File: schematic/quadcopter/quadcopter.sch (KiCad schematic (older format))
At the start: 17 parts, among them SW1 SW_SPST, U1 WEACT_STM32F411CEU6, U10 iFlight_XING_E_2207, U11 HAKRC_35A_ESC, U12 iFlight_XING_E_2207, U13 iFlight_XING_E_2207, U14 iFlight_XING_E_2207, U2 SPARKRUN_ICM-20948, U3 LIPO_Battery_4CELL, U4 FS-A8S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

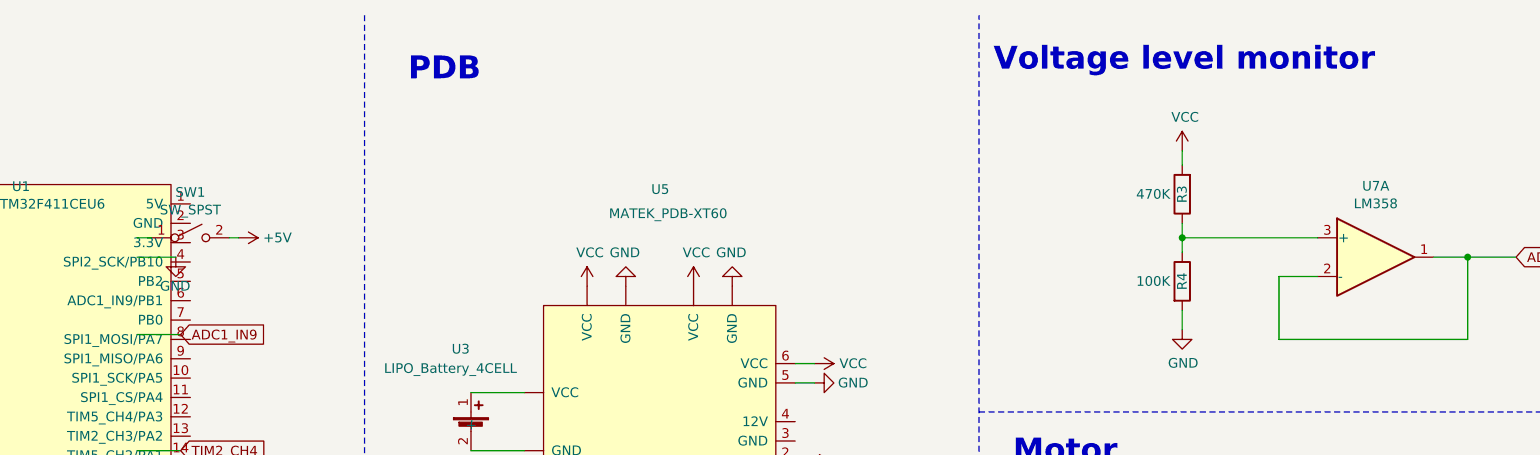
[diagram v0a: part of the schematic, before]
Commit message: Update voltage monitor
- delete moving average filter
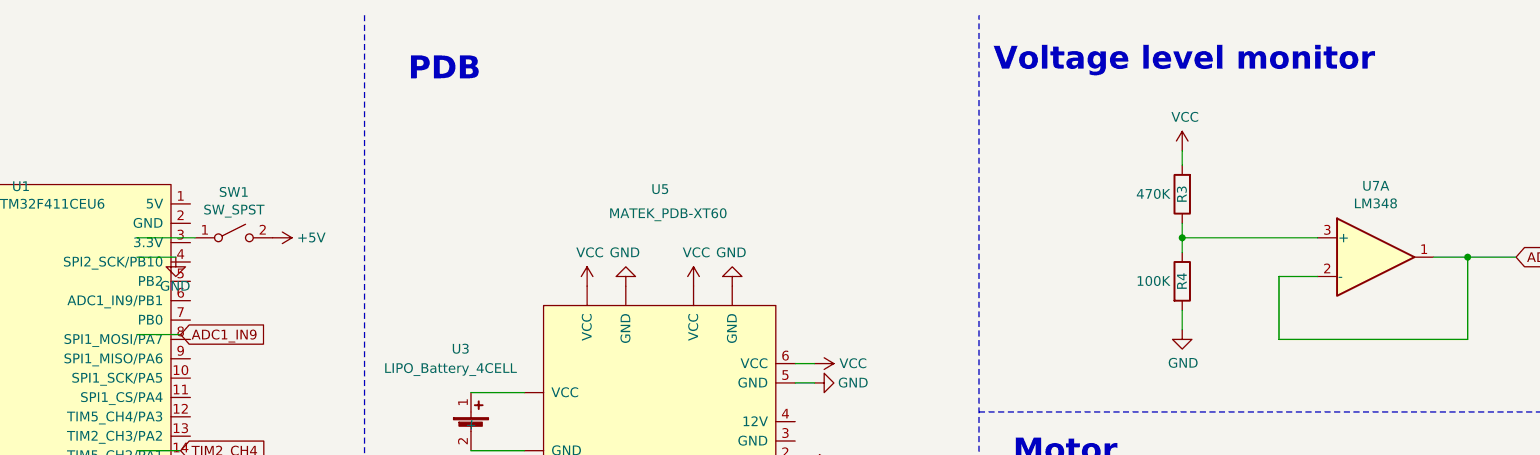
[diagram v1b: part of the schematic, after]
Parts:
- U7: value LM358 -> LM348
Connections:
- wire segments 75 -> 74
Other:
- moved on the sheet: SW1
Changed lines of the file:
@@
 L power:+5V #PWR0103
 U 1 1 606BF20D
-P 3150 1625
-F 0 "#PWR0103" H 3150 1475 50  0001 C CNN
-F 1 "+5V" V 3150 1825 50  0000 C CNN
-F 2 "" H 3150 1625 50  0001 C CNN
-F 3 "" H 3150 1625 50  0001 C CNN
-	1    3150 1625
+P 3325 1625
+F 0 "#PWR0103" H 3325 1475 50  0001 C CNN
+F 1 "+5V" V 3325 1825 50  0000 C CNN
+F 2 "" H 3325 1625 50  0001 C CNN
+F 3 "" H 3325 1625 50  0001 C CNN
+	1    3325 1625
 	0    1    1    0
 $EndComp
@@
 L Switch:SW_SPST SW1
 U 1 1 6075AD94
-P 2900 1625
-F 0 "SW1" H 2900 1860 50  0000 C CNN
-F 1 "SW_SPST" H 2900 1769 50  0000 C CNN
-F 2 "" H 2900 1625 50  0001 C CNN
-F 3 "~" H 2900 1625 50  0001 C CNN
-	1    2900 1625
-	1    0    0    -1
-$EndComp
-Wire Wire Line
-	2625 1625 2700 1625
-Wire Wire Line
-	3100 1625 3150 1625
+P 3125 1625
+F 0 "SW1" H 3125 1860 50  0000 C CNN
+F 1 "SW_SPST" H 3125 1769 50  0000 C CNN
+F 2 "" H 3125 1625 50  0001 C CNN
+F 3 "~" H 3125 1625 50  0001 C CNN
+	1    3125 1625
+	1    0    0    -1
+$EndComp
+Wire Wire Line
+	2625 1625 2925 1625
 Wire Wire Line
 	2625 1725 2825 1725
@@
 P 9025 1725
 F 0 "U7" H 9025 2092 50  0000 C CNN
-F 1 "LM358" H 9025 2001 50  0000 C CNN
+F 1 "LM348" H 9025 2001 50  0000 C CNN
 F 2 "" H 9025 1725 50  0001 C CNN
 F 3 "http://www.ti.com/lit/ds/symlink/lm2904-n.pdf" H 9025 1725 50  0001 C CNN

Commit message: Update FMU schematic
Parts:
- removed R3: 470K, symbol Device:R
- removed R4: 100K, symbol Device:R
- removed U1: WEACT_STM32F411CEU6, symbol quadcopter_symbol:WEACT_STM32F411CEU6
- removed U11, U6: HAKRC_35A_ESC, symbol quadcopter_symbol:HAKRC_35A_ESC
- removed U14: iFlight_XING_E_2207, symbol quadcopter_symbol:iFlight_XING_E_2207
- removed U2: SPARKRUN_ICM-20948, symbol quadcopter_symbol:SPARKRUN_ICM-20948
- removed U3: LIPO_Battery_4CELL, symbol quadcopter_symbol:LIPO_Battery_4CELL
- removed U4: FS-A8S, symbol quadcopter_symbol:FS-A8S
- removed U5: MATEK_PDB-XT60, symbol quadcopter_symbol:MATEK_PDB-XT60
- removed U7: LM348, symbol Amplifier_Operational:LM358
- added BZ1: Buzzer, symbol Device:Buzzer
- added R1: 470K, symbol Device:R
- added R2: 100K, symbol Device:R
- added U1: MATEK_PDB-XT60, symbol quadcopter_symbol:MATEK_PDB-XT60
- added U11: iFlight_XING_E_2207, symbol quadcopter_symbol:iFlight_XING_E_2207
- added U2: nRF24L01+PA+LNA_BreakOut, symbol quadcopter_symbol:nRF24L01+PA+LNA_BreakOut
- added U3: LM358N, symbol quadcopter_symbol:LM358N
- added U4: WEACT_STM32F411CEU6, symbol quadcopter_symbol:WEACT_STM32F411CEU6
- added U5, U7: HAKRC_35A_ESC, symbol quadcopter_symbol:HAKRC_35A_ESC
- added U6: ICM_20948_BreakOut, symbol quadcopter_symbol:ICM_20948_BreakOut
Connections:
- net labels added: +BATT, SWO
- net labels removed: +5V, ADC1_IN9, CS, MISO, MOSI, SCLK, SPI1_CS, SPI1_MISO, SPI1_MOSI, SPI1_SCLK, TIM2_CH3, TIM2_CH4, TIM5_CH1, TIM5_CH2, USART1_RX
- wire segments 74 -> 113
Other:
- note removed: "IMU (ICM-20948)"
- note removed: "MCU module"
- note removed: "Motor"
- note removed: "Motor 1"
- note removed: "Motor 2"
- note removed: "Motor 3"
- note removed: "Motor 4"
- note removed: "PDB"
- note removed: "RC Receiver (FS-A8S)"
- note removed: "Voltage level monitor"

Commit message: Update FMU schematic
- add 2 LED
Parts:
- added D1, D2: LED, symbol Device:LED
- added R3, R4: 330K, symbol Device:R
- added U14: ST-LINK, symbol quadcopter-rescue:ST-LINK
- U1: symbol quadcopter_symbol:MATEK_PDB-XT60 -> quadcopter-rescue:MATEK_PDB-XT60-quadcopter_symbol
- U10, U11, U12, U13: symbol quadcopter_symbol:iFlight_XING_E_2207 -> quadcopter-rescue:iFlight_XING_E_2207-quadcopter_symbol
- U2: symbol quadcopter_symbol:nRF24L01+PA+LNA_BreakOut -> quadcopter-rescue:nRF24L01+PA+LNA_BreakOut-quadcopter_symbol
- U3: symbol quadcopter_symbol:LM358N -> quadcopter-rescue:LM358N-quadcopter_symbol
- U4: symbol quadcopter_symbol:WEACT_STM32F411CEU6 -> quadcopter-rescue:WEACT_STM32F411CEU6-quadcopter_symbol
- U5, U7, U8, U9: symbol quadcopter_symbol:HAKRC_35A_ESC -> quadcopter-rescue:HAKRC_35A_ESC-quadcopter_symbol
- U6: symbol quadcopter_symbol:ICM_20948_BreakOut -> quadcopter-rescue:ICM_20948_BreakOut-quadcopter_symbol
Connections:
- net +3V3 is gone; now on an unnamed net: U4.1 (PB12/CE)
- net SWCLK is gone; now on an unnamed net: U4.3 (PB14/SPI2_MISO)
- net SWDIO is gone; now on an unnamed net: U4.2 (PB13/SPI2_CS)
- net SWO is gone; now on an unnamed net: U4.11 (SPI1_CS/PA4)
- net GND: no longer U4.4 (SPI2_SCK/PB10)
- net at U4.1 (PB12/CE): now also U14.3 (3.3V); no longer U6.2 (VIN)
- net at U4.10 (SPI1_SCK/PA5): now also U6.4 (SCLK)
- net at U6.4 (SCLK): no longer U4.10 (SPI1_SCK/PA5)
- net at U4.11 (SPI1_CS/PA4): now also U14.2 (SWO); no longer U6.6 (VIN)
- net at U4.12 (TIM5_CH4/PA3): now also U5.3 (Signal)
- net at U5.2 (Telemetry): now also U10.2; no longer U4.12 (TIM5_CH4/PA3)
- net at U4.13 (TIM2_CH3/PA2): now also U7.3 (Signal)
- net at U7.3 (Signal): now also U11.3; no longer U4.13 (TIM2_CH3/PA2)
- net at U4.14 (TIM5_CH2/PA1): now also U8.3 (Signal)
- net at U8.3 (Signal): now also U12.3; no longer U4.14 (TIM5_CH2/PA1)
- net at U4.15 (TIM2_CH1/PA0): now also U9.3 (Signal)
- net at U9.3 (Signal): now also U13.3; no longer U4.15 (TIM2_CH1/PA0)
- net at U4.18 (PC14): now also SW1.2 (B)
- net at U4.19 (PC13): now also BZ1.1 (-), R2.2, U1.1 (GND), U1.5 (GND), U2.1 (GND), U3.~ (VCC), D1.1 (K), D2.1 (K)
- net at U4.2 (PB13/SPI2_CS): now also U14.4 (SWDIO); no longer U6.1 (GND)
- net at U4.20 (VB): now also U2.2 (VCC)
- net at U4.3 (PB14/SPI2_MISO): now also U14.5 (SWCLK)
- net at U4.5 (PA8): now also R3.1
- net at U4.6 (PA9): now also R4.1
- net at U3.~ (VCC): no longer U4.6 (PA9)
- net at U4.7 (PA10/GPIO): now also U3.~ (VCC)
- net at U4.8 (SPI1_MOSI/PA7): now also U6.3 (MOSI)
- net at U6.3 (MOSI): no longer U4.8 (SPI1_MOSI/PA7)
- net at U4.9 (SPI1_MISO/PA6): now also U6.5 (MISO)
- net at U6.5 (MISO): no longer U4.9 (SPI1_MISO/PA6)
- net at SW1.1 (A), U1.2 (5V): now also U3.~ (VCC), U14.1 (5V)
- net at U5.3 (Signal): now also U10.3
- net at U7.2 (Telemetry): now also U11.2
- net at U8.2 (Telemetry): now also U12.2
- net at U9.2 (Telemetry): now also U13.2
- new net: U4.1 (PB12/CE), U6.2 (VIN)
- new net: U4.11 (SPI1_CS/PA4), U6.6 (VIN)
- new net: U4.2 (PB13/SPI2_CS), U6.1 (GND)
- new net: U14.6 (GND), U4.4 (SPI2_SCK/PB10)
- new net: D1.2 (A), R3.2
- new net: D2.2 (A), R4.2
- now unconnected: U3.~ (VCC), U3.~ (VCC)
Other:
- moved on the sheet: BZ1, R1, R2, SW1, U1, U10, U11, U12, U13, U2, U3, U4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
